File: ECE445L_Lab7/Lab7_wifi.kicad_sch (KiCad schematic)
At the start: 4 parts, among them U3 ESP8266-01/ESP-01

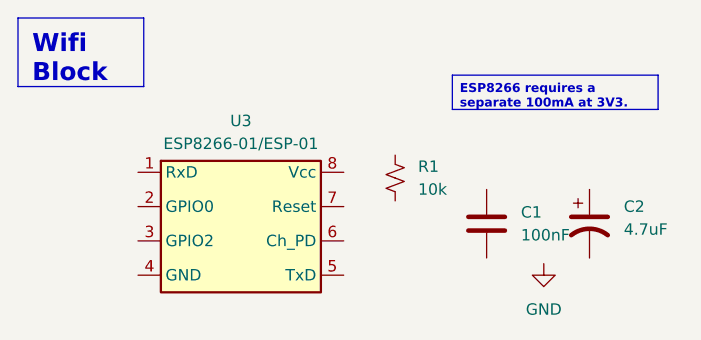
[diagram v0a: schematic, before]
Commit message: update all symbols and re-sync footprints in the KiCad projects
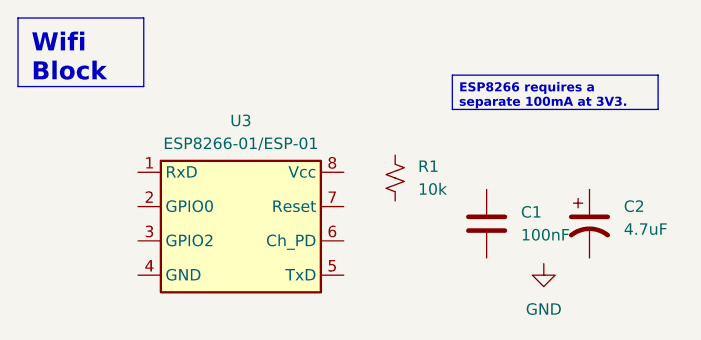
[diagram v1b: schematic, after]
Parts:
- U3: footprint ECE445L:PinHeader_2x04_P2.54mm_Vertical -> ECE445L:ESP8266_FemaleConnector
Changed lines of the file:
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@@
 (kicad_sch
-	(version 20231120)
+	(version 20250114)
 	(generator "eeschema")
-	(generator_version "8.0")
+	(generator_version "9.0")
 	(paper "A4")
 	(text_box "ESP8266 requires a separate 100mA at 3V3."
@@
 		(at 97.155 42.545 0)
 		(size 22.86 3.81)
+		(margins 0.75 0.75 0.75 0.75)
 		(stroke
 			(width 0)
@@
 		(at 48.895 36.195 0)
 		(size 13.97 7.62)
+		(margins 1.5 1.5 1.5 1.5)
 		(stroke
 			(width 0)
@@
 			)
 		)
-		(property "Footprint" "ECE445L:PinHeader_2x04_P2.54mm_Vertical"
+		(property "Footprint" "ECE445L:ESP8266_FemaleConnector"
 			(at 73.025 66.675 0)
 			(effects
